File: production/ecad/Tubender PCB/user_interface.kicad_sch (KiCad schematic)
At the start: 34 parts, among them IC1 74HC4050D, IC2 RA8875L3N, IC3 SN74LVC1G29DCTR, J7 4-1734592-0, U5 74HC595, U6 PEC11R-4215K-S0024

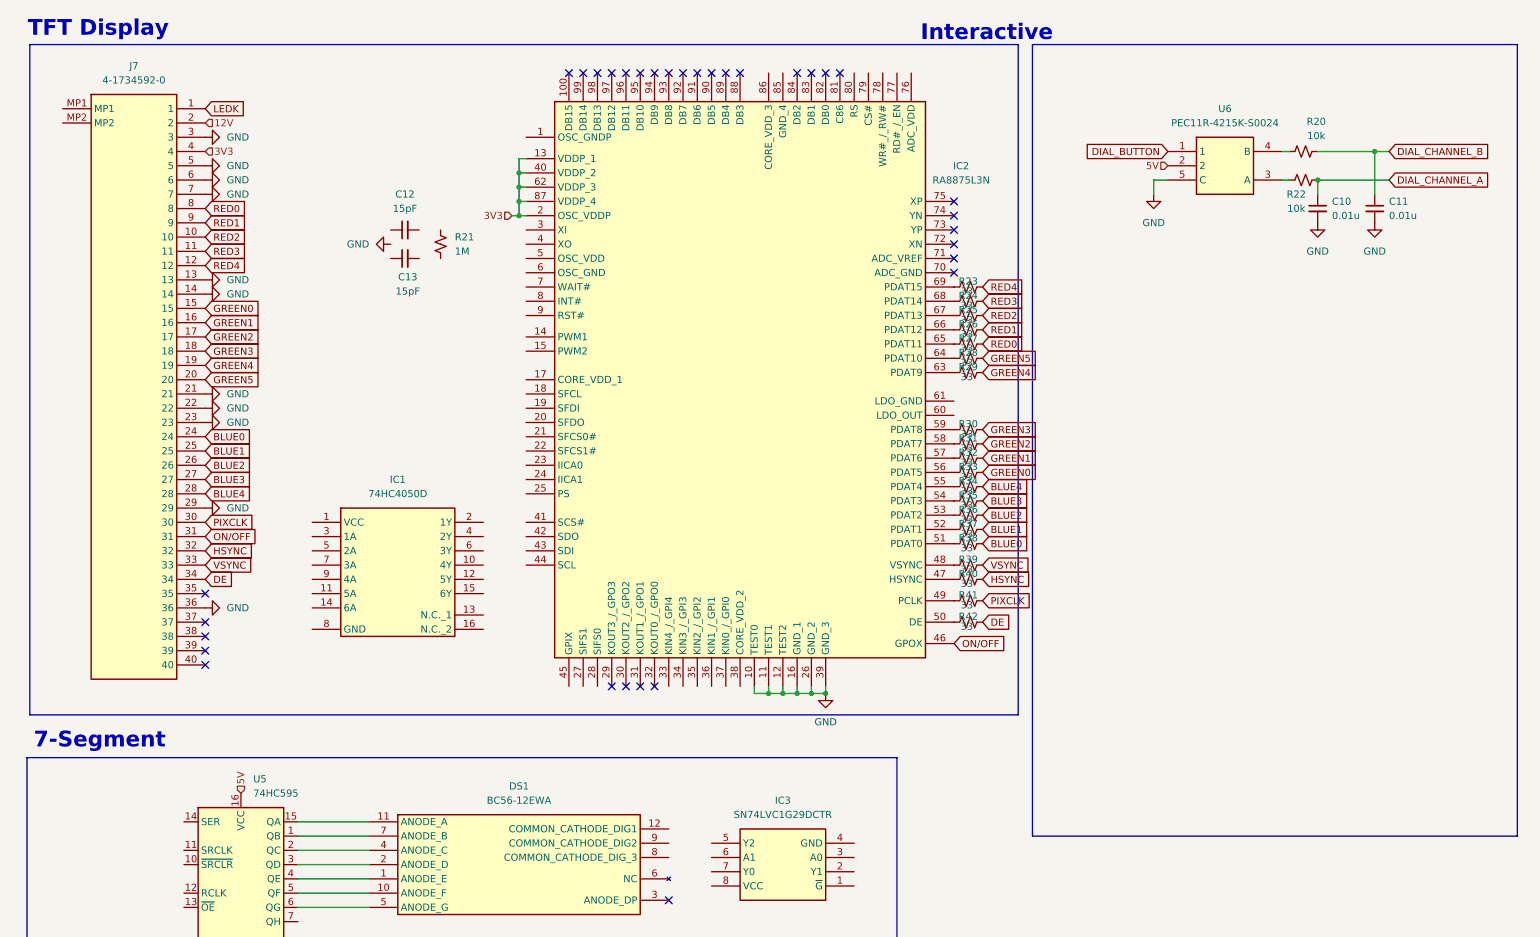
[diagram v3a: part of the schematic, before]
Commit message: Completed RA8875 Driver
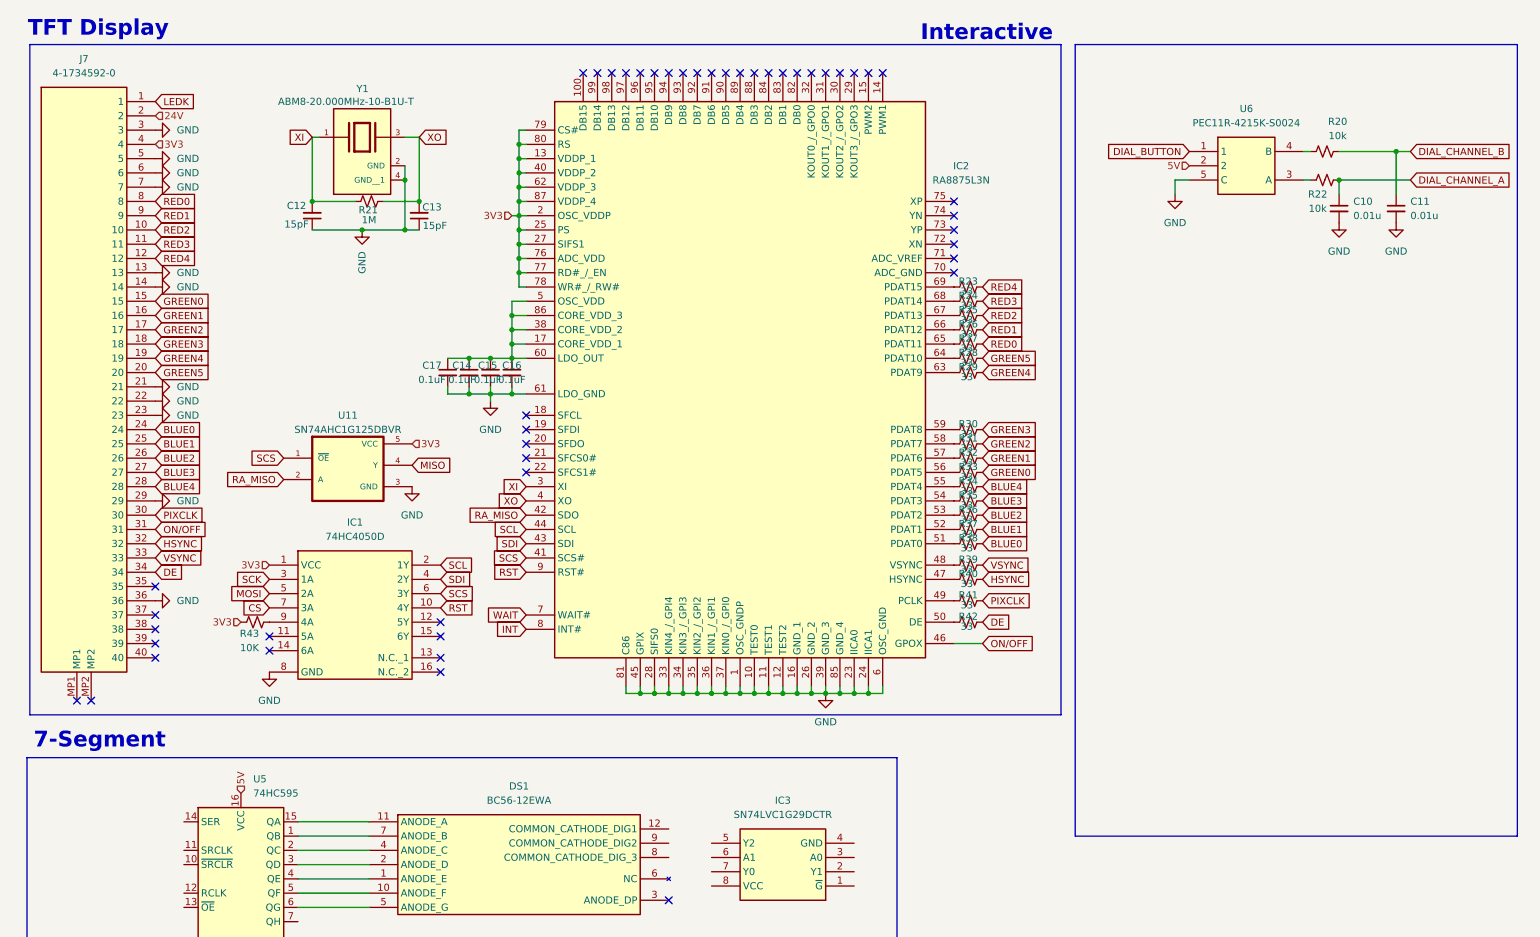
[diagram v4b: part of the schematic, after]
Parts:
- added C14, C15, C16, C17: 0.1uF, symbol Device:C_Small
- added R43: 10K, symbol Device:R_Small_US
- added U11: SN74AHC1G125DBVR, SN74AHC1G125DBVR:SOT95P280X145-5N, symbol SN74AHC1G125DBVR:SN74AHC1G125DBVR
- added Y1: ABM8-20.000MHz-10-B1U-T, ABM8-20.000MHz-10-B1U-T:XTAL_ABM8-20.000MHz-10-B1U-T, symbol ABM8-20.000MHz-10-B1U-T:ABM8-20.000MHz-10-B1U-T
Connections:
- net 3V3: now also IC1.1 (VCC), IC2.25 (PS), IC2.27 (SIFS1), IC2.76 (ADC_VDD), IC2.77 (RD#_/_EN), IC2.78 (WR#_/_RW#), IC2.79 (CS#), IC2.80 (RS), R43.2, U11.5 (VCC)
- net GND: now also C12.1, C13.1, IC1.8 (GND), IC2.1 (OSC_GNDP), IC2.23 (IICA0), IC2.24 (IICA1), IC2.28 (SIFS0), IC2.33 (KIN4_/_GPI4), IC2.34 (KIN3_/_GPI3), IC2.35 (KIN2_/_GPI2), IC2.36 (KIN1_/_GPI1), IC2.37 (KIN0_/_GPI0), IC2.45 (GPIX), IC2.6 (OSC_GND), IC2.61 (LDO_GND), IC2.81 (C86), IC2.85 (GND_4), C14.2, C15.2, C16.2, C17.2, U11.3 (GND), Y1.2 (GND), Y1.4 (GND__1)
- net XI: now reaches C12.2
- net XI: now also IC2.3 (XI), R21.1, Y1.1
- net XO: now reaches R21.2
- net XO: now also C13.2, IC2.4 (XO), Y1.3
- net at IC2.17 (CORE_VDD_1): now also IC2.38 (CORE_VDD_2), IC2.5 (OSC_VDD), IC2.60 (LDO_OUT), IC2.86 (CORE_VDD_3), C14.1, C15.1, C16.1, C17.1
- net SCS: now reaches IC2.41 (SCS#)
- net SCS: now also IC1.6 (3Y), U11.1 (~{OE})
- net RA_MISO: now reaches IC2.42 (SDO)
- net RA_MISO: now also U11.2 (A)
- net SDI: now reaches IC2.43 (SDI)
- net SDI: now also IC1.4 (2Y)
- net SCL: now reaches IC2.44 (SCL)
- net SCL: now also IC1.2 (1Y)
- net WAIT: now reaches IC2.7 (WAIT#)
- net INT: now reaches IC2.8 (INT#)
- net RST: now reaches IC2.9 (RST#)
- net RST: now also IC1.10 (4Y)
- net SCK: now reaches IC1.3 (1A)
- net MOSI: now reaches IC1.5 (2A)
- net CS: now reaches IC1.7 (3A)
- net at IC1.9 (4A): now also R43.1
- net 12V renamed 24V
- new net MISO: U11.4 (Y)
- no-connect marks 33 -> 47
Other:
- moved on the sheet: C10, C11, C12, C13, IC1, J7, R20, R21, R22, U6

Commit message: final for rev 1
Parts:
- added C18: 0.1uF, symbol Device:C
- added U8, U9: CD4051BE, CD4051BE:DIP794W45P254L1969H508Q16, symbol CD4051BE:CD4051BE
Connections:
- net 3V3: now also U5.10 (~{SRCLR}), U8.16 (VDD), U9.16 (VDD)
- net 5V: now also IC3.8 (VCC), C18.1
- net GND: now also IC3.4 (GND), C18.2, U8.6 (INH), U8.7 (VEE), U8.8 (VSS), U9.6 (INH), U9.7 (VEE), U9.8 (VSS)
- net 7-SEG_SRCLK: now reaches U5.11 (SRCLK)
- net 7-SEG_RCLK: now reaches U5.12 (RCLK)
- net 7-SEG_OEb: now reaches U5.13 (~{OE})
- net 7-SEG_SER: now reaches U5.14 (SER)
- net 7-SEG_Gb: now reaches IC3.1 (~{G})
- net at IC3.2 (Y1): now also DS1.9 (COMMON_CATHODE_DIG2)
- net 7-SEG_A0: now reaches IC3.3 (A0)
- net 7-SEG_A1: now reaches IC3.5 (Y2)
- net 7-SEG_A1: now also DS1.8 (COMMON_CATHODE_DIG_3), IC3.6 (A1)
- net at IC3.7 (Y0): now also DS1.12 (COMMON_CATHODE_DIG1)
- new net BUTTON_0: U8.13 (CHANNELS_IN/OUT_0)
- new net BUTTON_1: U8.14 (CHANNELS_IN/OUT_1)
- new net BUTTON_10: U9.15 (CHANNELS_IN/OUT_2)
- new net BUTTON_11: U9.12 (CHANNELS_IN/OUT_3)
- new net BUTTON_12: U9.1 (CHANNELS_IN/OUT_4)
- new net BUTTON_13: U9.5 (CHANNELS_IN/OUT_5)
- new net BUTTON_14: U9.2 (CHANNELS_IN/OUT_6)
- new net BUTTON_15: U9.4 (CHANNELS_IN/OUT_7)
- new net BUTTON_2: U8.15 (CHANNELS_IN/OUT_2)
- new net BUTTON_3: U8.12 (CHANNELS_IN/OUT_3)
- new net BUTTON_4: U8.1 (CHANNELS_IN/OUT_4)
- new net BUTTON_5: U8.5 (CHANNELS_IN/OUT_5)
- new net BUTTON_6: U8.2 (CHANNELS_IN/OUT_6)
- new net BUTTON_7: U8.4 (CHANNELS_IN/OUT_7)
- new net BUTTON_8: U9.13 (CHANNELS_IN/OUT_0)
- new net BUTTON_9: U9.14 (CHANNELS_IN/OUT_1)
- new net BUTTON_CHAN_SEL_1A: U8.11 (A)
- new net BUTTON_CHAN_SEL_1B: U8.10 (B)
- new net BUTTON_CHAN_SEL_1C: U8.9 (C)
- new net BUTTON_CHAN_SEL_2A: U9.11 (A)
- new net BUTTON_CHAN_SEL_2B: U9.10 (B)
- new net BUTTON_CHAN_SEL_2C: U9.9 (C)
- new net BUTTON_PLEX_1: U8.3 (COM_OUT/IN)
- new net BUTTON_PLEX_2: U9.3 (COM_OUT/IN)
- no-connect marks 47 -> 50

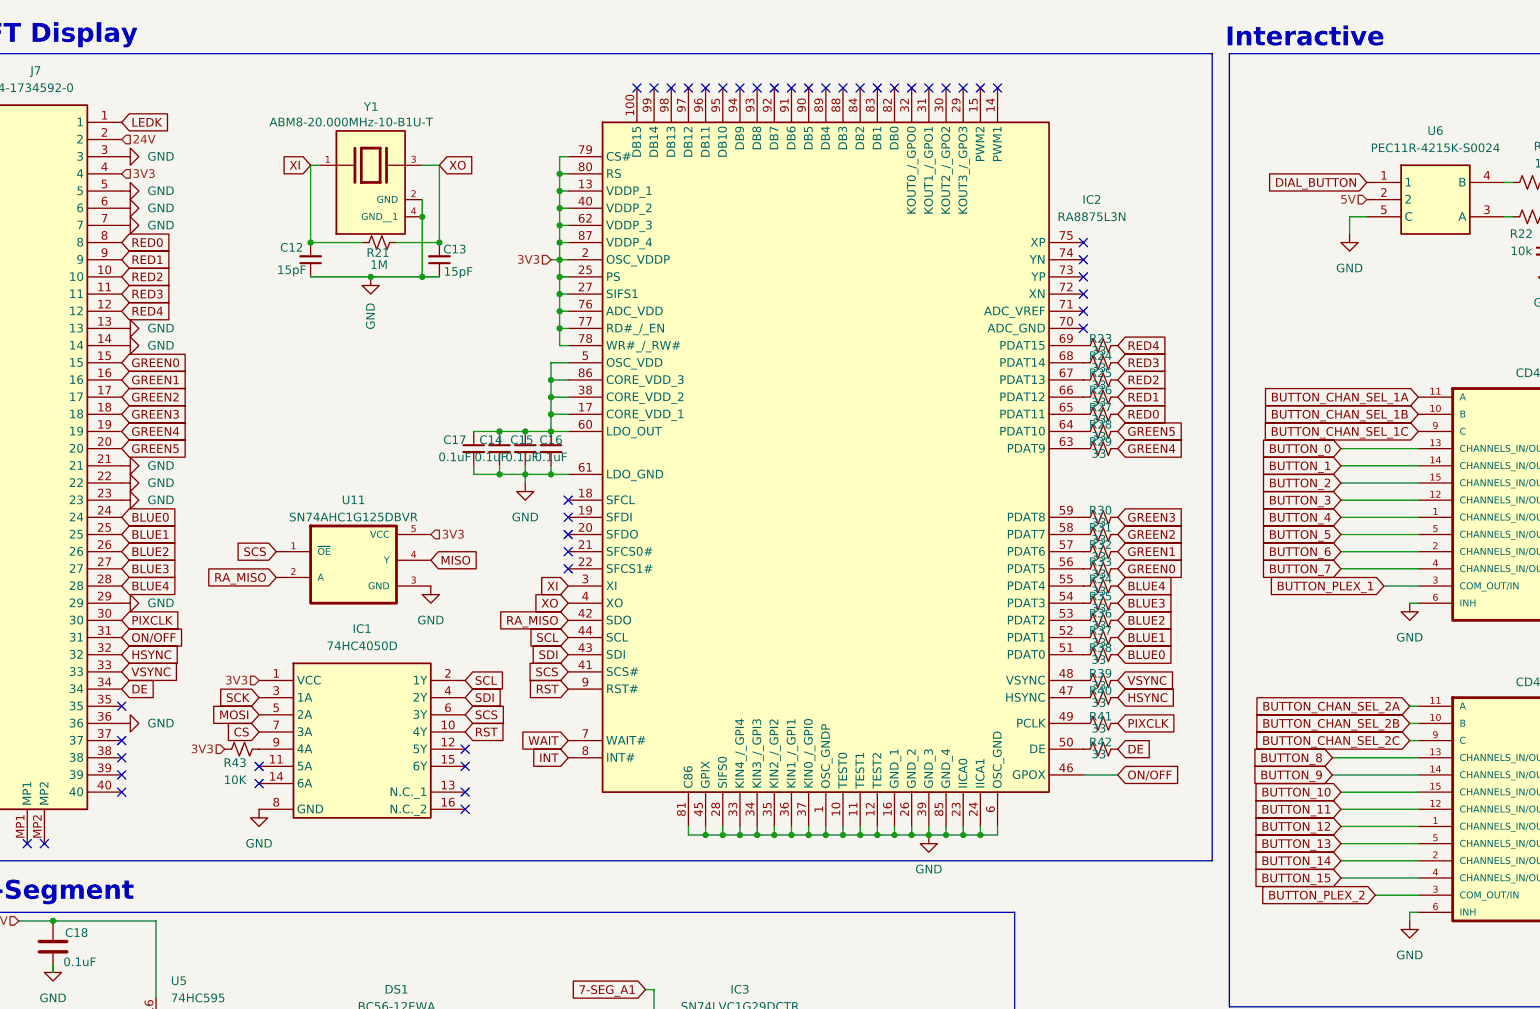
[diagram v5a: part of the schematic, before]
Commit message: Display to MCU
Forgot to add global nets for display to the control page, my b
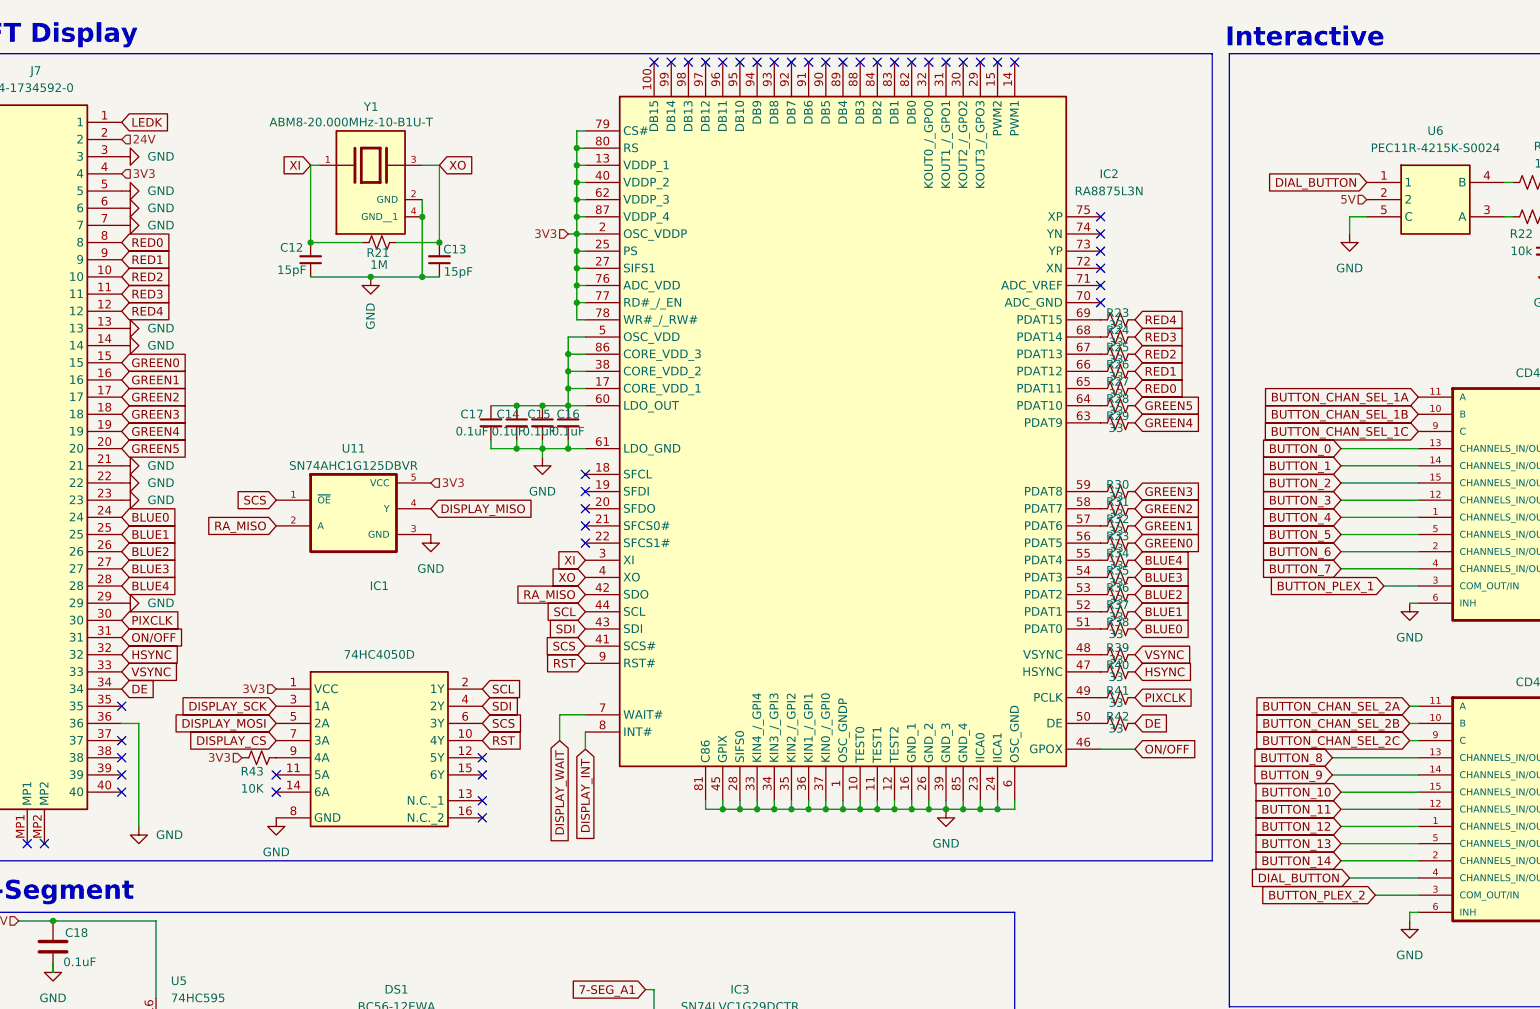
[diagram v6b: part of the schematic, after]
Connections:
- net BUTTON_15 is gone; now on net DIAL_BUTTON: U9.4 (CHANNELS_IN/OUT_7)
- net CS renamed DISPLAY_CS
- net INT renamed DISPLAY_INT
- net MISO renamed DISPLAY_MISO
- net MOSI renamed DISPLAY_MOSI
- net SCK renamed DISPLAY_SCK
- net WAIT renamed DISPLAY_WAIT
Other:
- moved on the sheet: C14, C15, C16, C17, IC1, IC2, R23, R24, R25, R26, R27, R28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

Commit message: Fixed Button Connectors
All done! Enjoy :)
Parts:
- added J12, J15, J16, J17, J18, J19, J20, J21, J22, J23, J24, J25, J26, J27, J28: 640387-2, 640387-2:TE_640387-2, symbol 640387-2:640387-2
- added J29: 640387-5, 640387-5:TE_640387-5, symbol 640387-5:640387-5
- added R49, R50, R51, R52, R53, R54, R55, R56, R57, R58, R59, R60, R61, R62, R63: 10k, symbol Device:R_US
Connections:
- net 3V3: now also R49.2, R50.2, R51.2, R52.2, R53.2, R54.2, R55.2, R56.2, R57.2, R58.2, R59.2, R60.2, R61.2, R62.2, R63.2
- net 5V: now also J29.1
- net BUTTON_0: now also J12.1, R49.1
- net BUTTON_1: now also J15.1, R50.1
- net BUTTON_10: now also J24.1, R59.1
- net BUTTON_12: now also J26.1, R61.1
- net BUTTON_13: now also J27.1, R62.1
- net BUTTON_14: now also J28.1, R63.1
- net BUTTON_2: now also J16.1, R51.1
- net BUTTON_3: now also J17.1, R52.1
- net BUTTON_4: now also J18.1, R53.1
- net BUTTON_5: now also J19.1, R54.1
- net BUTTON_6: now also J21.1, R56.1
- net BUTTON_7: now also J20.1, R55.1
- net BUTTON_8: now also J22.1, R57.1
- net BUTTON_9: now also J23.1, R58.1
- net DIAL_BUTTON: now also J29.2
- net DIAL_CHANNEL_A: now also J29.4
- net DIAL_CHANNEL_B: now also J29.3
- net GND: now also J12.2, J15.2, J16.2, J17.2, J18.2, J19.2, J20.2, J21.2, J22.2, J23.2, J24.2, J25.2, J26.2, J27.2, J28.2, J29.5
- new net: J25.1, R60.1
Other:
- note added: "Buttons"
- moved on the sheet: C10, C11, C12, C13, C14, C15, C16, C17, C18, DS1, IC1, IC2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

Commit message: Moved Display SPI to MCU VSPI and Organized UI Sheet
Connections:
- net 24V renamed +24V
- net 3V3 renamed +3V3
- net +3V3: no longer IC2.76 (ADC_VDD)
- net 5V renamed +5V
- no-connect marks 50 -> 51
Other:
- note added: "INPUTS"
- note added: "MUX"
- note added: "POWER"
- note added: "Rotary Encoder"
- note removed: "Interactive"
- moved on the sheet: C10, C11, C12, C13, C14, C15, C16, C17, IC1, IC2, J7, R20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
